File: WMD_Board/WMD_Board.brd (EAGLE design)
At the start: 75.7 x 43.7 mm, 74 parts, among them IC1 FGPMMOPA6H, J1 EMPCB.SMAFSTJ.B.HT, J2 5015680607, Q1 SI2323DS-T1-E3, Q2 SI2323DS-T1-E3, Q3 SI2312BDS, U1 STM32L053C8T6, U2 BSS138, U3 RFM69HCW, U4 BSS138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

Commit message: Routed
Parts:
- removed C5: 0.1uF, SparkFun-Capacitors:0603
- removed LED1: (no value), led:CHIP-LED0805
- removed R14, R15: 10k, SparkFun-Resistors:0603
- removed R2: 1k, SparkFun-Resistors:0603
- moved R8 117.6 mm to (6.10, 26.0), flipped to the bottom
- moved R7 113.4 mm to (6.10, 27.8), flipped to the bottom, turned to 180 degrees
- moved RESET 63.6 mm to (40.4, 9.02), turned to 180 degrees
- moved C18 63.1 mm to (57.5, 17.8)
- moved R3 61.1 mm to (48.1, 21.8), turned to 90 degrees
- moved C17 58.7 mm to (38.4, 11.9)
- moved C21 58.3 mm to (29.8, 24.6), flipped to the top, turned to 270 degrees
- moved Y2 56.3 mm to (53.1, 17.8)
- moved R4 56.0 mm to (41.8, 20.2)
- moved U2 55.9 mm to (38.6, 20.2)
- moved U$10 55.4 mm to (51.6, 20.2)
- moved R5 53.6 mm to (34.6, 20.3), turned to 0 degrees
- moved U6 53.5 mm to (32.8, 24.6), flipped to the top, turned to 0 degrees
- moved C13 52.6 mm to (57.5, 19.4), turned to 180 degrees
- moved C20 52.6 mm to (35.7, 24.7), flipped to the top, turned to 270 degrees
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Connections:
- removed net BTN4: C5.1, R15.1, U1.13
- removed net BTN4_OUT: R14.1, R15.2, U$20.8
- removed net N$1: R2.2, U1.39
- removed net N$5: LED1.A, R2.1
- net 3.3V: no longer R14.2
- net BTN2: now also U1.45; no longer U1.11
- net BTN3: now also U1.46; no longer U1.12
- net GND: no longer C5.2, LED1.C, U$10.VSS@2
- net HR_MFIO: now also U1.38; no longer U$10.MFIO@2, U1.40
- net SDA_TO_HR_SENSOR: no longer U$10.SENSOR_SDA@2
- net SHUTDOWN: now also U1.12; no longer U1.2
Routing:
- net 3.3V: track 18.3 -> 242.9 mm, vias 4 -> 19
- net 1.8V: track 0.00 -> 95.5 mm, vias 0 -> 2
- net GPS_TX: track 0.00 -> 55.6 mm
- net GPS_RX: track 0.00 -> 54.4 mm
- net BTN_POWER_OUT: track 0.00 -> 46.9 mm, vias 0 -> 3
- net HR_RESET: track 0.00 -> 46.1 mm, vias 0 -> 4
- net NRST: track 0.00 -> 43.7 mm, vias 0 -> 2
- net GPS_NRST: track 0.00 -> 42.1 mm
- net LORA_MISO: track 0.00 -> 41.2 mm, vias 0 -> 2
- net WC_EEPROM: track 0.00 -> 38.8 mm
- net LORA_SCK: track 0.00 -> 38.6 mm, vias 0 -> 2
- net LORA_CS: track 0.00 -> 37.6 mm
- net LORA_DIO5: track 0.00 -> 37.0 mm
- net LORA_MOSI: track 0.00 -> 35.6 mm, vias 0 -> 2
- net BTN3: track 0.00 -> 31.3 mm, vias 0 -> 3
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- added copper zone on layer 16, net 3.3V

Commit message: Ground Vias and Silkscreen
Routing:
- net GND: vias 23 -> 39
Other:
- board text added: "MARS WMD_Board v1"
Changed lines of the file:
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@@
 <setting verticaltext="up"/>
 </settings>
-<grid distance="5" unitdist="mil" unit="mil" style="lines" multiple="1" display="yes" altdistance="5" altunitdist="mil" altunit="mil"/>
+<grid distance="10" unitdist="mil" unit="mil" style="lines" multiple="1" display="yes" altdistance="5" altunitdist="mil" altunit="mil"/>
 <layers>
 <layer number="1" name="Top" color="4" fill="1" visible="yes" active="yes"/>
@@
 <hole x="41.402" y="4.572" drill="1.27"/>
 <hole x="2.032" y="26.797" drill="1.27"/>
+<text x="15.24" y="29.718" size="1.524" layer="21">MARS WMD_Board v1</text>
 </plain>
 <attributes>
@@
 <attribute name="MF" value="STMicroelectronics" x="3.556" y="14.478" size="1.778" layer="27" rot="R90" display="off"/>
 <attribute name="MP" value="M24512-DRMN8TP/K" x="3.556" y="14.478" size="1.778" layer="27" rot="R90" display="off"/>
-<attribute name="NAME" x="0.869" y="10.558" size="1.27" layer="25" rot="R90"/>
+<attribute name="NAME" x="7.473" y="14.368" size="1.27" layer="25" rot="R90"/>
 <attribute name="PACKAGE" value="SOIC-8 STMicroelectronics" x="3.556" y="14.478" size="1.778" layer="27" rot="R90" display="off"/>
 <attribute name="PRICE" value="None" x="3.556" y="14.478" size="1.778" layer="27" rot="R90" display="off"/>
@@
 <via x="45.339" y="21.209" extent="1-16" drill="0.35"/>
 <via x="45.339" y="19.812" extent="1-16" drill="0.35"/>
-<via x="66.675" y="29.337" extent="1-16" drill="0.35"/>
-<via x="66.675" y="26.543" extent="1-16" drill="0.35"/>
+<via x="66.675" y="29.845" extent="1-16" drill="0.35"/>
+<via x="66.675" y="26.289" extent="1-16" drill="0.35"/>
 <via x="52.07" y="34.29" extent="1-16" drill="0.35"/>
 <via x="55.88" y="30.48" extent="1-16" drill="0.35"/>
 <via x="59.69" y="34.29" extent="1-16" drill="0.35"/>
-<via x="55.88" y="40.64" extent="1-16" drill="0.35"/>
+<via x="55.626" y="40.386" extent="1-16" drill="0.35"/>
 <via x="45.593" y="14.732" extent="1-16" drill="0.35"/>
 <via x="54.991" y="17.145" extent="1-16" drill="0.35"/>
+<via x="1.524" y="30.988" extent="1-16" drill="0.35"/>
+<via x="7.62" y="30.988" extent="1-16" drill="0.35"/>
+<via x="11.938" y="30.988" extent="1-16" drill="0.35"/>
+<via x="2.794" y="23.114" extent="1-16" drill="0.35"/>
+<via x="7.112" y="23.114" extent="1-16" drill="0.35"/>
+<via x="8.128" y="17.78" extent="1-16" drill="0.35"/>
+<via x="8.89" y="12.446" extent="1-16" drill="0.35"/>
+<via x="20.828" y="10.922" extent="1-16" drill="0.35"/>
+<via x="25.4" y="10.922" extent="1-16" drill="0.35"/>
+<via x="30.226" y="10.922" extent="1-16" drill="0.35"/>
+<via x="34.544" y="10.922" extent="1-16" drill="0.35"/>
+<via x="52.07" y="2.794" extent="1-16" drill="0.35"/>
+<via x="55.626" y="6.096" extent="1-16" drill="0.35"/>
+<via x="59.182" y="2.794" extent="1-16" drill="0.35"/>
+<via x="25.908" y="21.336" extent="1-16" drill="0.35"/>
+<via x="29.972" y="19.304" extent="1-16" drill="0.35"/>
 </signal>
 <signal name="3.3V">

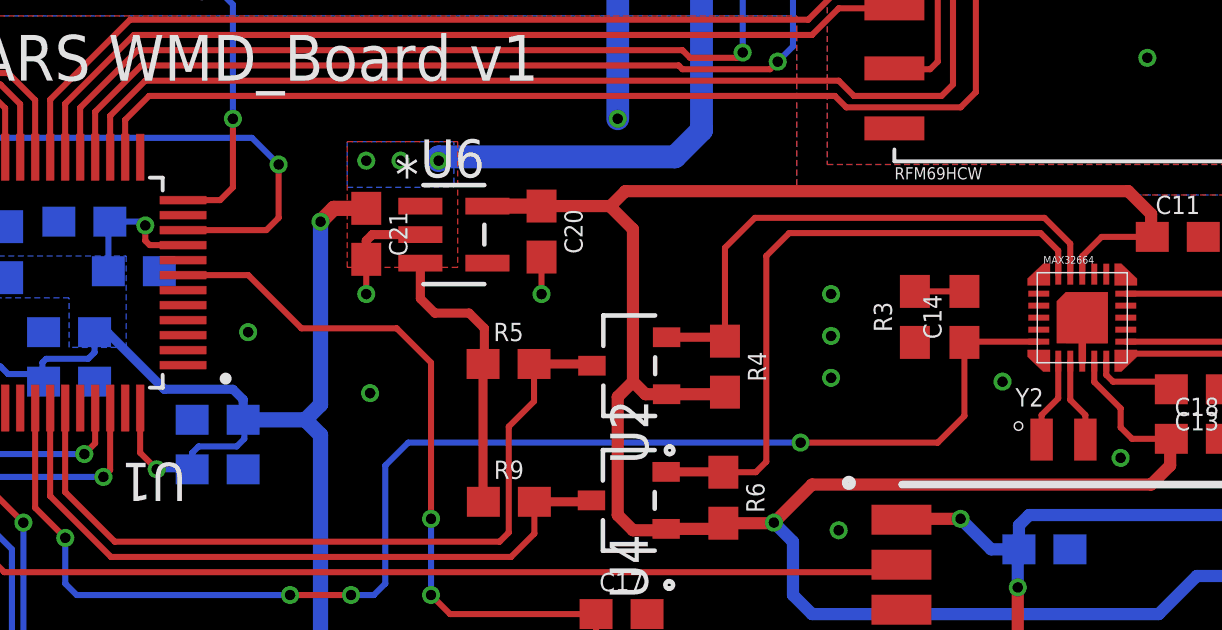
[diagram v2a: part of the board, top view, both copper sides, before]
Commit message: Routed MFIO Pin (routing completed)
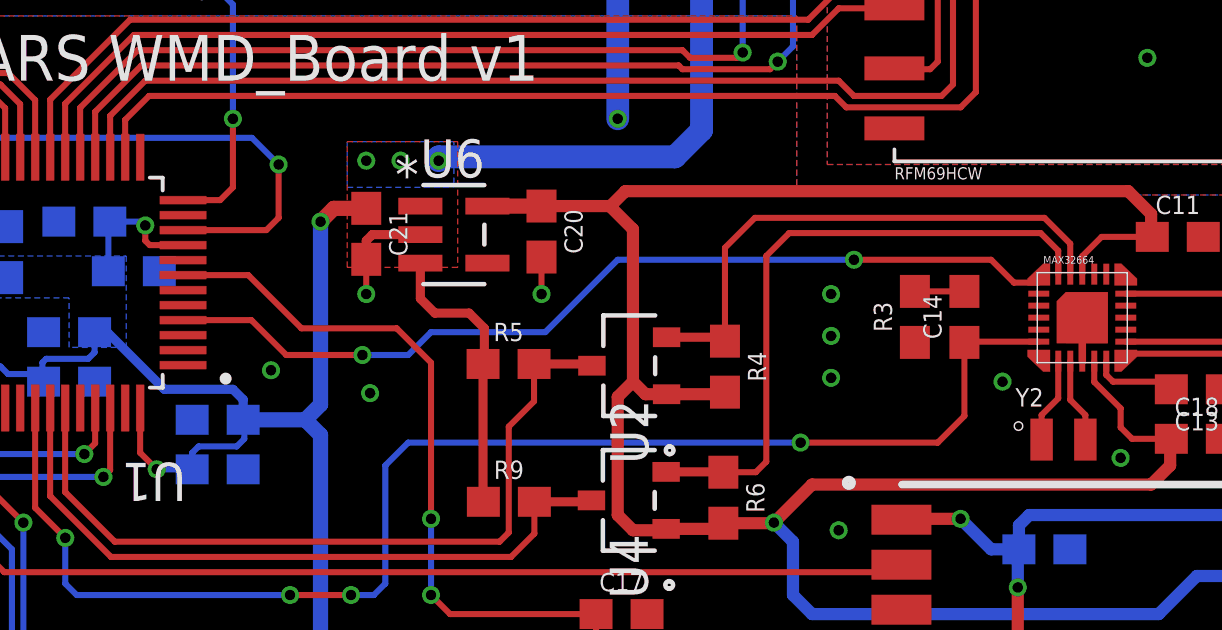
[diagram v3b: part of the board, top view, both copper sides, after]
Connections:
- net HR_MFIO: now also U1.4; no longer U1.38
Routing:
- net HR_MFIO: track 0.00 -> 30.6 mm, vias 0 -> 2
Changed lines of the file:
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@@
 <setting verticaltext="up"/>
 </settings>
-<grid distance="10" unitdist="mil" unit="mil" style="lines" multiple="1" display="yes" altdistance="5" altunitdist="mil" altunit="mil"/>
+<grid distance="5" unitdist="mil" unit="mil" style="lines" multiple="1" display="yes" altdistance="5" altunitdist="mil" altunit="mil"/>
 <layers>
 <layer number="1" name="Top" color="4" fill="1" visible="yes" active="yes"/>
@@
 <layer number="17" name="Pads" color="2" fill="1" visible="yes" active="yes"/>
 <layer number="18" name="Vias" color="2" fill="1" visible="yes" active="yes"/>
-<layer number="19" name="Unrouted" color="6" fill="1" visible="no" active="yes"/>
+<layer number="19" name="Unrouted" color="6" fill="1" visible="yes" active="yes"/>
 <layer number="20" name="Dimension" color="24" fill="1" visible="yes" active="yes"/>
 <layer number="21" name="tPlace" color="7" fill="1" visible="yes" active="yes"/>
@@
 <via x="55.626" y="6.096" extent="1-16" drill="0.35"/>
 <via x="59.182" y="2.794" extent="1-16" drill="0.35"/>
-<via x="25.908" y="21.336" extent="1-16" drill="0.35"/>
+<via x="26.67" y="20.066" extent="1-16" drill="0.35"/>
 <via x="29.972" y="19.304" extent="1-16" drill="0.35"/>
 </signal>
@@
 <signal name="HR_MFIO">
 <contactref element="U$10" pad="MFIO@1"/>
-<contactref element="U1" pad="38"/>
-<wire x1="17.308" y1="18.807" x2="52.262" y2="23.0184" width="0" layer="19" extent="1-1"/>
+<contactref element="U1" pad="4"/>
+<wire x1="23.738" y1="21.737" x2="26.015" y2="21.737" width="0.2032" layer="1"/>
+<wire x1="26.015" y1="21.737" x2="27.178" y2="20.574" width="0.2032" layer="1"/>
+<wire x1="27.178" y1="20.574" x2="29.718" y2="20.574" width="0.2032" layer="1"/>
+<via x="29.718" y="20.574" extent="1-16" drill="0.35"/>
+<wire x1="29.718" y1="20.574" x2="31.242" y2="20.574" width="0.2032" layer="16"/>
+<via x="46.101" y="23.749" extent="1-16" drill="0.35"/>
+<wire x1="46.101" y1="23.749" x2="50.673" y2="23.749" width="0.2032" layer="1"/>
+<wire x1="50.673" y1="23.749" x2="51.435" y2="22.987" width="0.2032" layer="1"/>
+<wire x1="51.435" y1="22.987" x2="52.2306" y2="22.987" width="0.2032" layer="1"/>
+<wire x1="52.2306" y1="22.987" x2="52.262" y2="23.0184" width="0.2032" layer="1"/>
+<wire x1="31.242" y1="20.574" x2="32.004" y2="21.336" width="0.2032" layer="16"/>
+<wire x1="32.004" y1="21.336" x2="35.814" y2="21.336" width="0.2032" layer="16"/>
+<wire x1="35.814" y1="21.336" x2="38.227" y2="23.749" width="0.2032" layer="16"/>
+<wire x1="38.227" y1="23.749" x2="46.101" y2="23.749" width="0.2032" layer="16"/>
 </signal>
 <signal name="N$10">

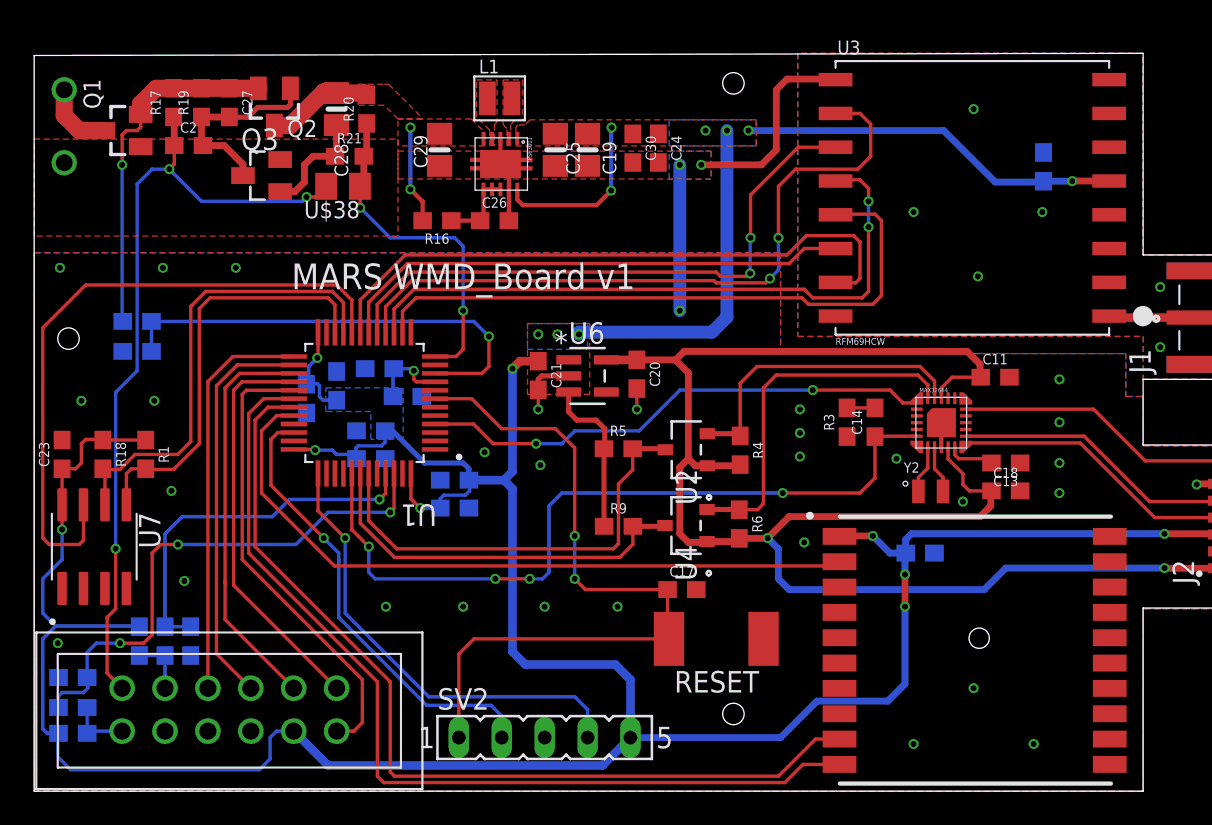
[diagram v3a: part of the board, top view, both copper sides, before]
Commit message: hole spacing
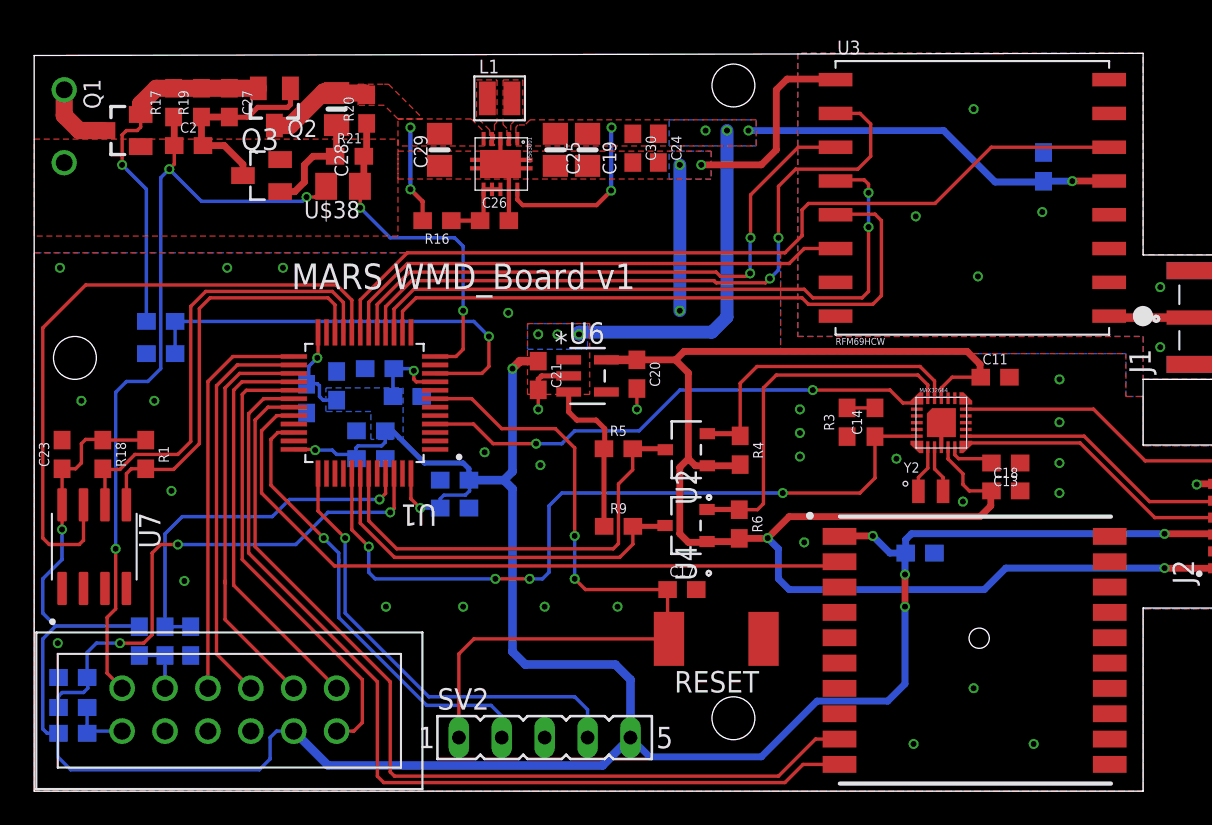
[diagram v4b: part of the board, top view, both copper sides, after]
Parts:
- moved R8 1.40 mm to (7.49, 25.9)
- moved R7 1.40 mm to (7.49, 27.8)
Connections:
- removed net DIO0: U3.6P
- new net LORA_DIO0: U1.19, U3.6P
- net LORA_DIO5: no longer U1.19
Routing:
- net LORA_DIO0: track 0.00 -> 50.9 mm
- net LORA_DIO5: track 37.0 -> 0.00 mm
- net N$4: track 27.3 -> 26.0 mm
- net 3.3V: track 242.9 -> 243.9 mm
- net MEASURE: track 21.1 -> 21.7 mm
- net GND: vias 39 -> 40

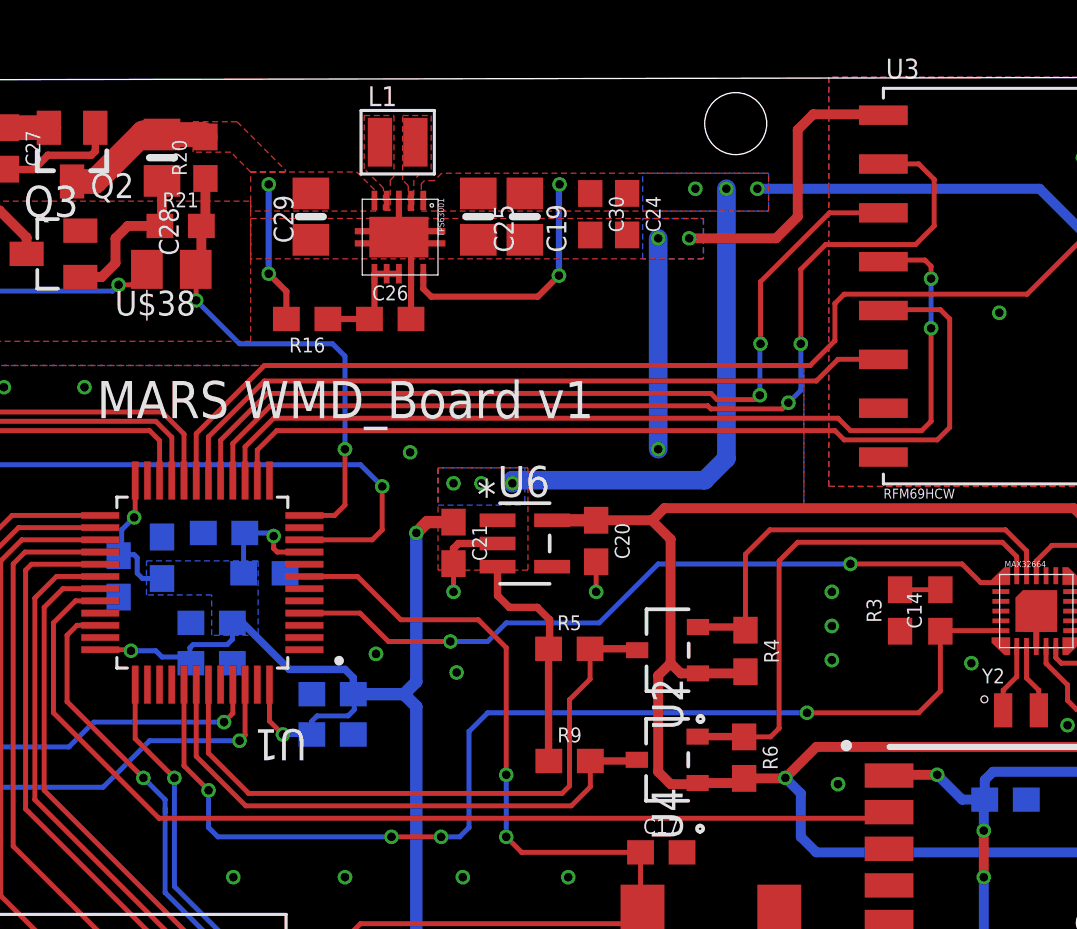
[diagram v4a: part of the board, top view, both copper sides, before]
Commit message: added heartbeat led, ferrite bead, pin breakout
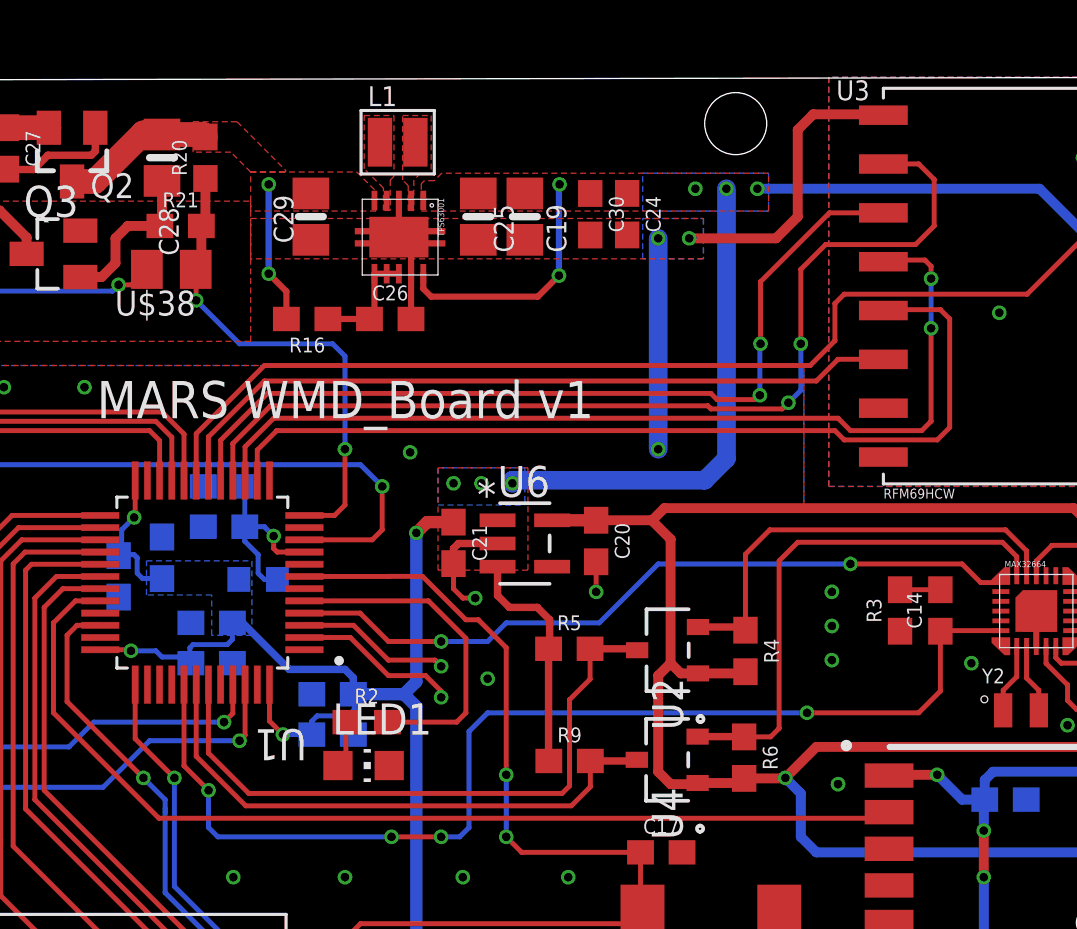
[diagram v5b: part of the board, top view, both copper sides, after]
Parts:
- added FB1: FERRITE_BEAD, Ferrite_Bead:BEADC1608X100N
- added LED1: (no value), led:CHIP-LED0805
- added R2: 1k, SparkFun-Resistors:0603
- moved C1 2.52 mm to (20.4, 25.3), turned to 0 degrees
- moved C6 1.91 mm to (20.4, 26.9)
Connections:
- new net BO1: U1.3
- new net BO2: U1.2
- new net N$1: LED1.A, R2.1
- new net N$12: R2.2, U1.5
- new net N$5: C1.1, C6.1, FB1.2, U1.9
- net 3.3V: now also FB1.1; no longer C1.1, C6.1, U1.9
- net GND: now also LED1.C
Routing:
- net N$12: track 0.00 -> 13.7 mm
- net N$5: track 0.00 -> 7.85 mm, vias 0 -> 1
- net BO2: track 0.00 -> 6.76 mm, vias 0 -> 1
- net BO1: track 0.00 -> 6.29 mm, vias 0 -> 1
- net 3.3V: track 243.9 -> 239.1 mm, vias 19 -> 18
- net N$1: track 0.00 -> 1.91 mm
- net GND: track 33.7 -> 34.6 mm, vias 40 -> 39
